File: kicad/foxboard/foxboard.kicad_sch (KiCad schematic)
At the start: 178 parts, among them J2 USB_C_Receptacle_USB2.0, K1 KEYSW, K10 KEYSW, K11 KEYSW, K12 KEYSW, K13 KEYSW, K14 KEYSW, K15 KEYSW, K16 KEYSW, K17 KEYSW, K18 KEYSW, K19 KEYSW, K2 KEYSW, K20 KEYSW, K21 KEYSW, K22 KEYSW, K23 KEYSW, K24 KEYSW, K25 KEYSW, K26 KEYSW, K27 KEYSW, K28 KEYSW, K29 KEYSW, K3 KEYSW, K30 KEYSW, K31 KEYSW, K32 KEYSW, K33 KEYSW, K34 KEYSW, K35 KEYSW, K36 KEYSW, K37 KEYSW, K38 KEYSW, K39 KEYSW, K4 KEYSW, K40 KEYSW, K41 KEYSW, K42 KEYSW, K43 KEYSW, K44 KEYSW, K45 KEYSW, K46 KEYSW, K47 KEYSW, K48 KEYSW, K49 KEYSW, K5 KEYSW, K50 KEYSW, K51 KEYSW, K52 KEYSW, K53 KEYSW, K54 KEYSW, K55 KEYSW, K56 KEYSW, K57 KEYSW, K58 KEYSW, K59 KEYSW, K6 KEYSW, K60 KEYSW, K61 KEYSW, K62 KEYSW, K63 KEYSW, K64 KEYSW, K65 KEYSW, K66 KEYSW, K67 KEYSW, K68 KEYSW, K69 KEYSW, K7 KEYSW, K70 KEYSW, K71 KEYSW, K72 KEYSW, K73 KEYSW, K74 KEYSW, K75 KEYSW, K76 KEYSW, K77 KEYSW, K78 KEYSW, K79 KEYSW, K8 KEYSW, K80 KEYSW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

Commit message: switch to better layout
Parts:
- added S30: BACKSPACE, PCM_marbastlib-mx:STAB_MX_2u, symbol PCM_marbastlib-mx:MX_stab
- added S63: ANSI_ENTER, PCM_marbastlib-mx:STAB_MX_2.25u, symbol PCM_marbastlib-mx:MX_stab
- added S64: LShift, PCM_marbastlib-mx:STAB_MX_2.25u, symbol PCM_marbastlib-mx:MX_stab
- added S75: RSHIFT, PCM_marbastlib-mx:STAB_MX_P_2.75u, symbol PCM_marbastlib-mx:MX_stab
- added S80: 7u_SPACE, PCM_marbastlib-mx:STAB_MX_P_6.25u, symbol PCM_marbastlib-mx:MX_stab
- K1, K2, K3, K5, K6, K7, K8: footprint PCM_marbastlib-mx:SW_MX_1.25u -> PCM_marbastlib-mx:SW_MX_1u
- K15, K77, K78, K79, K81, K82, K83, K9: footprint PCM_marbastlib-mx:SW_MX_1u -> PCM_marbastlib-mx:SW_MX_1.25u
- K34, K47: footprint PCM_marbastlib-mx:SW_MX_1u -> PCM_marbastlib-mx:SW_MX_1.5u
- K38: footprint PCM_marbastlib-mx:SW_MX_1.75u -> PCM_marbastlib-mx:SW_MX_1u
- K4: footprint rhais_cherry:MX_KEY_4.45 -> PCM_marbastlib-mx:SW_MX_1u
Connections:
- net row 4: now reaches D55.1 (K), D56.1 (K), D57.1 (K), D58.1 (K), D59.1 (K), D60.1 (K), D61.1 (K), D62.1 (K), D63.1 (K)
- net row 4: now also D51.1 (K), D52.1 (K), D53.1 (K), D54.1 (K), U2.25 (33_MCLK2); no longer D64.1 (K), D65.1 (K), D66.1 (K), D67.1 (K), D68.1 (K), D69.1 (K), D70.1 (K), D87.1 (K), U2.26 (34_RX8)
- net row 2: now reaches D25.1 (K), D26.1 (K), D27.1 (K), D28.1 (K), D29.1 (K), D30.1 (K), D31.1 (K), D32.1 (K), D33.1 (K)
- net row 2: now also D17.1 (K), D18.1 (K), D19.1 (K), D20.1 (K), D21.1 (K), D22.1 (K), D23.1 (K), D24.1 (K), U2.45 (23_A9_CRX1_MCLK1); no longer D34.1 (K), D35.1 (K), D36.1 (K), D37.1 (K), U2.17 (25_A11_RX6_SDA2)
- net row 6: now reaches D77.1 (K), D78.1 (K), D79.1 (K), D80.1 (K), D81.1 (K), D82.1 (K), D83.1 (K), D84.1 (K), D85.1 (K), D86.1 (K)
- net row 6: now also D87.1 (K), U2.1 (GND); no longer D71.1 (K), D72.1 (K), D73.1 (K), D74.1 (K), D75.1 (K), D76.1 (K), U2.25 (33_MCLK2)
- net row 5: now reaches U2.2 (0_RX1_CRX2_CS1)
- net row 5: now also D64.1 (K), D65.1 (K), D66.1 (K), D67.1 (K), D68.1 (K), D69.1 (K), D70.1 (K), D71.1 (K), D72.1 (K), D73.1 (K), D74.1 (K), D75.1 (K), D76.1 (K)
- net row 3: now reaches D38.1 (K), D39.1 (K), D40.1 (K), D41.1 (K), D42.1 (K), D43.1 (K), D44.1 (K), D45.1 (K), D46.1 (K), D47.1 (K), D48.1 (K), D49.1 (K), D50.1 (K)
- net row 3: now also D34.1 (K), D35.1 (K), D36.1 (K), D37.1 (K), U2.44 (22_A8_CTX1); no longer D51.1 (K), D52.1 (K), D53.1 (K), D54.1 (K), U2.22 (30_CRX3)
- net row 1: now reaches D1.1 (K), D10.1 (K), D11.1 (K), D2.1 (K), D3.1 (K), D4.1 (K), D5.1 (K), D6.1 (K), D7.1 (K), D8.1 (K), D9.1 (K)
- net row 1: now also D12.1 (K), D13.1 (K), D14.1 (K), D15.1 (K), D16.1 (K), U2.46 (3V3); no longer U2.24 (32_OUT1B)
- net col 1: now reaches U2.3 (1_TX1_CTX2_MISO1)
- net col 1: now also K1.1, K17.1, K34.1, K51.1, K64.1, K77.1
- net col 3: now reaches U2.4 (2_OUT2)
- net col 3: now also K19.1, K2.1, K36.1, K53.1, K66.1, K79.1
- new net: D9.2 (A), K9.2
- new net col 10: K26.1, K43.1, K60.1, K73.1, K81.1, K9.1, U2.19 (27_A13_SCK1)
- new net col 11: K10.1, K27.1, K44.1, K61.1, K74.1, K82.1, U2.27 (35_TX8)
- new net col 12: K11.1, K28.1, K45.1, K62.1, U2.28 (36_CS)
- new net col 13: K12.1, K29.1, K46.1, K63.1, K75.1, K83.1, U2.29 (37_CS)
- new net col 14: K13.1, K30.1, K47.1, K84.1, U2.18 (26_A12_MOSI1)
- new net col 15: K14.1, K31.1, K48.1, K85.1, U2.31 (39_MISO1_OUT1A)
- new net col 16: K15.1, K32.1, K49.1, K76.1, K86.1, U2.36 (14_A0_TX3_SPDIF_OUT)
- new net col 17: K16.1, K33.1, K50.1, K87.1, U2.14 (12_MISO_MQSL)
- new net col 2: K18.1, K35.1, K52.1, K65.1, K78.1, U2.26 (34_RX8)
- new net col 4: K20.1, K3.1, K37.1, K54.1, K67.1, U2.24 (32_OUT1B)
- new net col 5: K21.1, K38.1, K4.1, K55.1, K68.1, U2.23 (31_CTX3)
- new net col 6: K22.1, K39.1, K5.1, K56.1, K69.1, K80.1, U2.22 (30_CRX3)
- new net col 7: K23.1, K40.1, K57.1, K6.1, K70.1, U2.21 (29_TX7)
- new net col 8: K24.1, K41.1, K58.1, K7.1, K71.1, U2.20 (28_RX7)
- new net col 9: K25.1, K42.1, K59.1, K72.1, K8.1, U2.30 (38_CS1_IN1)
- now unconnected: U2.15 (3V3), U2.16 (24_A10_TX6_SCL2), U2.32 (40_A16), U2.33 (41_A17), U2.34 (GND), U2.35 (13_SCK_LED)

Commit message: use usbc 2.0 recepticale
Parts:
- J2: footprint Connector_USB:USB_C_Receptacle_Amphenol_12401548E4-2A -> Connector_USB:USB_C_Receptacle_HRO_TYPE-C-31-M-12
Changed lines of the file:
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@@
       (effects (font (size 1.27 1.27)) (justify right))
     )
-    (property "Footprint" "Connector_USB:USB_C_Receptacle_Amphenol_12401548E4-2A" (at 271.78 166.37 0)
+    (property "Footprint" "Connector_USB:USB_C_Receptacle_HRO_TYPE-C-31-M-12" (at 271.78 166.37 0)
       (effects (font (size 1.27 1.27)) hide)
     )

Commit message: update
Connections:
- net row 1: now also U2.45 (23_A9_CRX1_MCLK1); no longer U2.46 (3V3)
- net row 2: now also U2.44 (22_A8_CTX1); no longer U2.45 (23_A9_CRX1_MCLK1)
- net row 3: now also U2.43 (21_A7_RX5_BCLK1); no longer U2.44 (22_A8_CTX1)

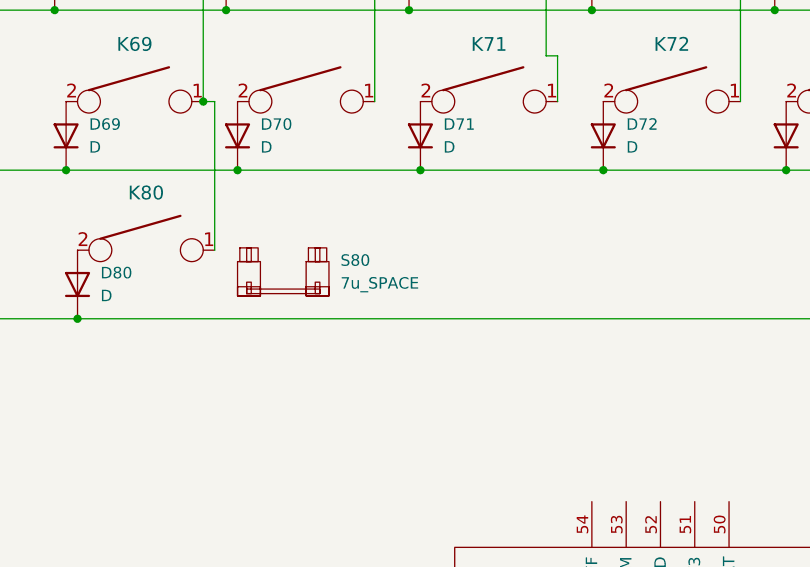
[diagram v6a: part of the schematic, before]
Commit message: add footprint for SOD882D & RESC168X55N
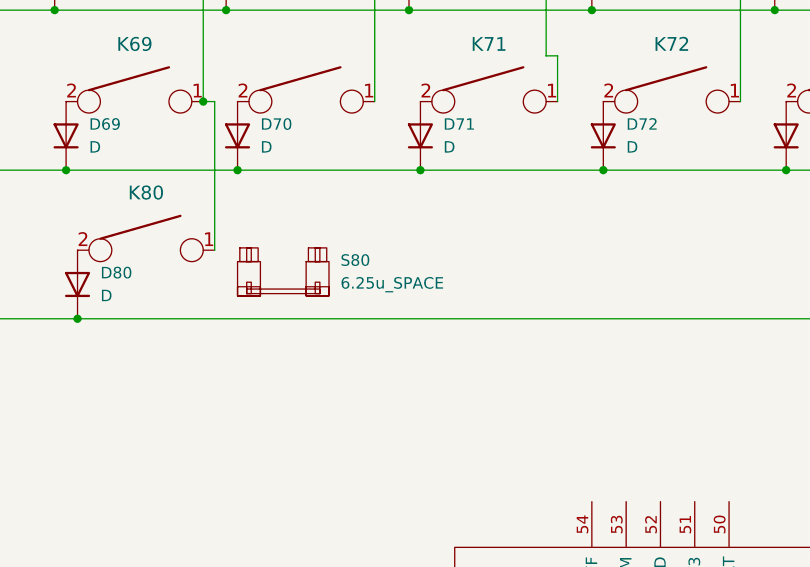
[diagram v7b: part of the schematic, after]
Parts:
- D1, D10, D11, D12, D13, D14, D15, D16, D17, D18, D19, D2, D20, D21, D22, D23, D24, D25, D26, D27, D28, D29, D3, D30, D31, D32, D33, D34, D35, D36, D37, D38, D39, D4, D40, D41, D42, D43, D44, D45, D46, D47, D48, D49, D5, D50, D51, D52, D53, D54, D55, D56, D57, D58, D59, D6, D60, D61, D62, D63, D64, D65, D66, D67, D68, D69, D7, D70, D71, D72, D73, D74, D75, D76, D77, D78, D79, D8, D80, D81, D82, D83, D84, D85, D86, D87, D9: footprint Diode_SMD:D_0201_0603Metric_Pad0.64x0.40mm_HandSolder -> custom:SOD882D
- R5, R6: footprint Resistor_SMD:R_0805_2012Metric_Pad1.20x1.40mm_HandSolder -> custom:RESC1608X55N
- S80: value 7u_SPACE -> 6.25u_SPACE

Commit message: update deps
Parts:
- D1, D10, D11, D12, D13, D14, D15, D16, D17, D18, D19, D2, D20, D21, D22, D23, D24, D25, D26, D27, D28, D29, D3, D30, D31, D32, D33, D34, D35, D36, D37, D38, D39, D4, D40, D41, D42, D43, D44, D45, D46, D47, D48, D49, D5, D50, D51, D53, D54, D55, D57, D58, D59, D6, D60, D61, D62, D63, D64, D65, D66, D67, D68, D69, D7, D70, D71, D72, D73, D74, D75, D76, D77, D78, D79, D8, D80, D81, D82, D83, D84, D85, D86, D87, D9: footprint custom:SOD882D -> Diode_SMD:D_SOD-323; MPN (none) -> C24372
- D52: footprint custom:SOD882D -> Diode_SMD:D_SOD-323; MPN (none) -> C2875153
- D56: footprint custom:SOD882D -> Diode_SMD:D_SOD-323;  MPN (none) -> C24372
- J2: MPN (none) -> C165948
- R5, R6: MPN (none) -> C416112
